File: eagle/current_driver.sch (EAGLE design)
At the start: 46 parts, among them IC4 UA78M05DCY, J1 Hall_Stop, J10 S5, J11 S1, J12 S2, J2 SIG_TEST, J3 S3, J9 S4, K2 4052, Q1 60V/32A/35mΩ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

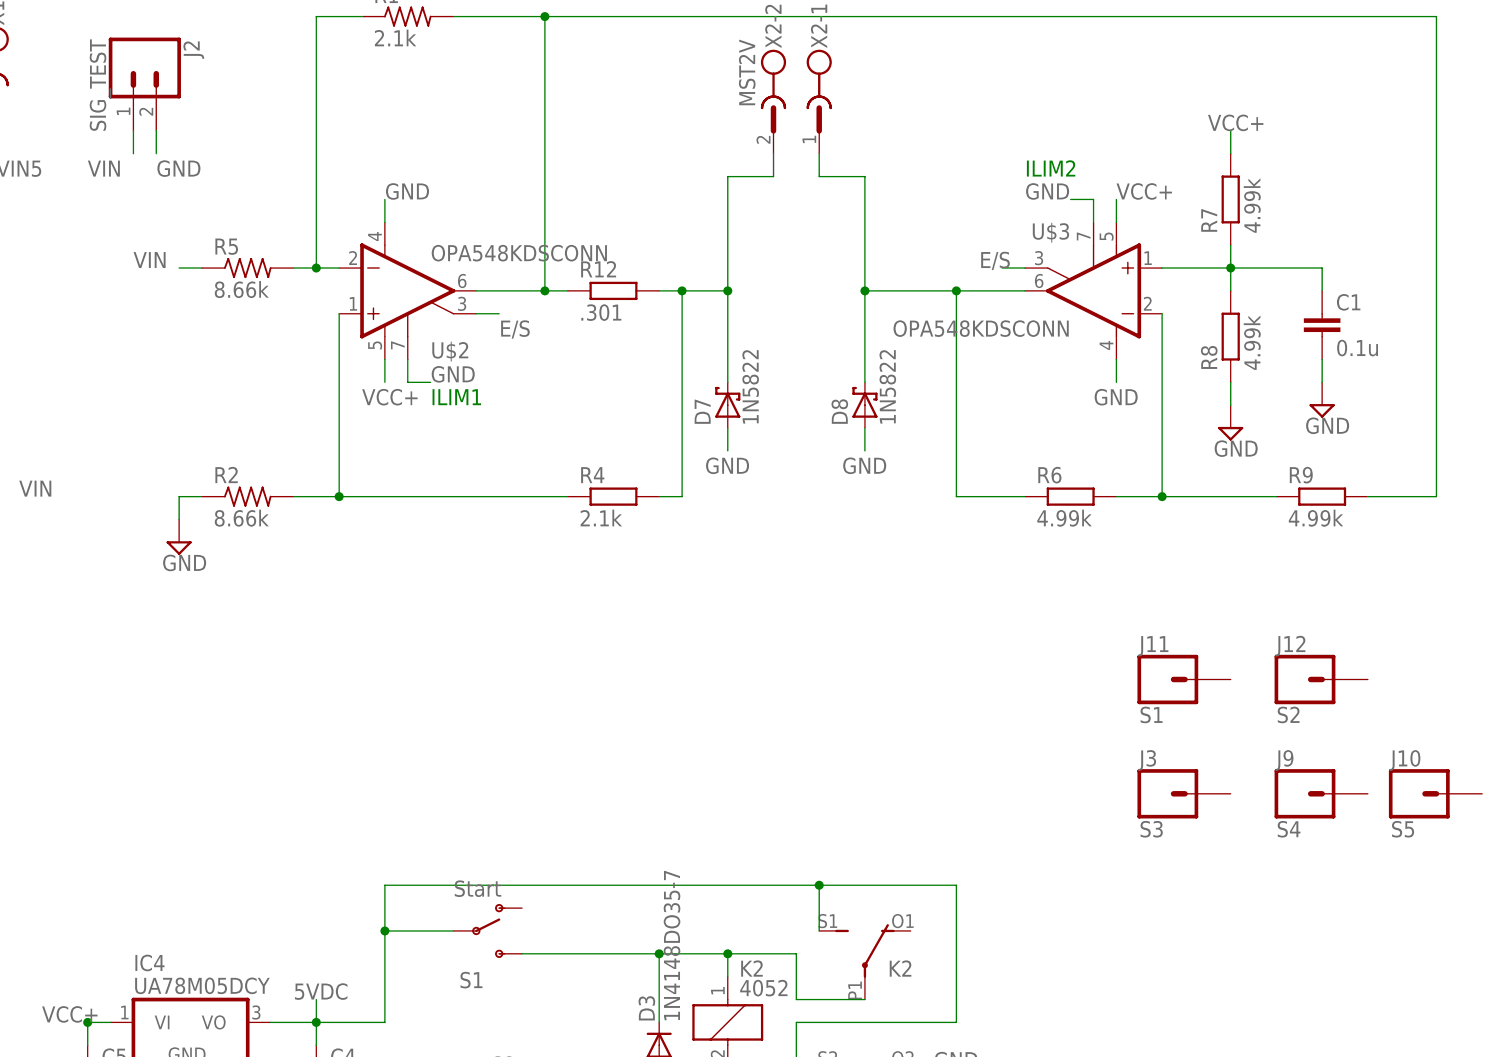
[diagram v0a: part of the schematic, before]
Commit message: modified Rs current sense resistor footprint
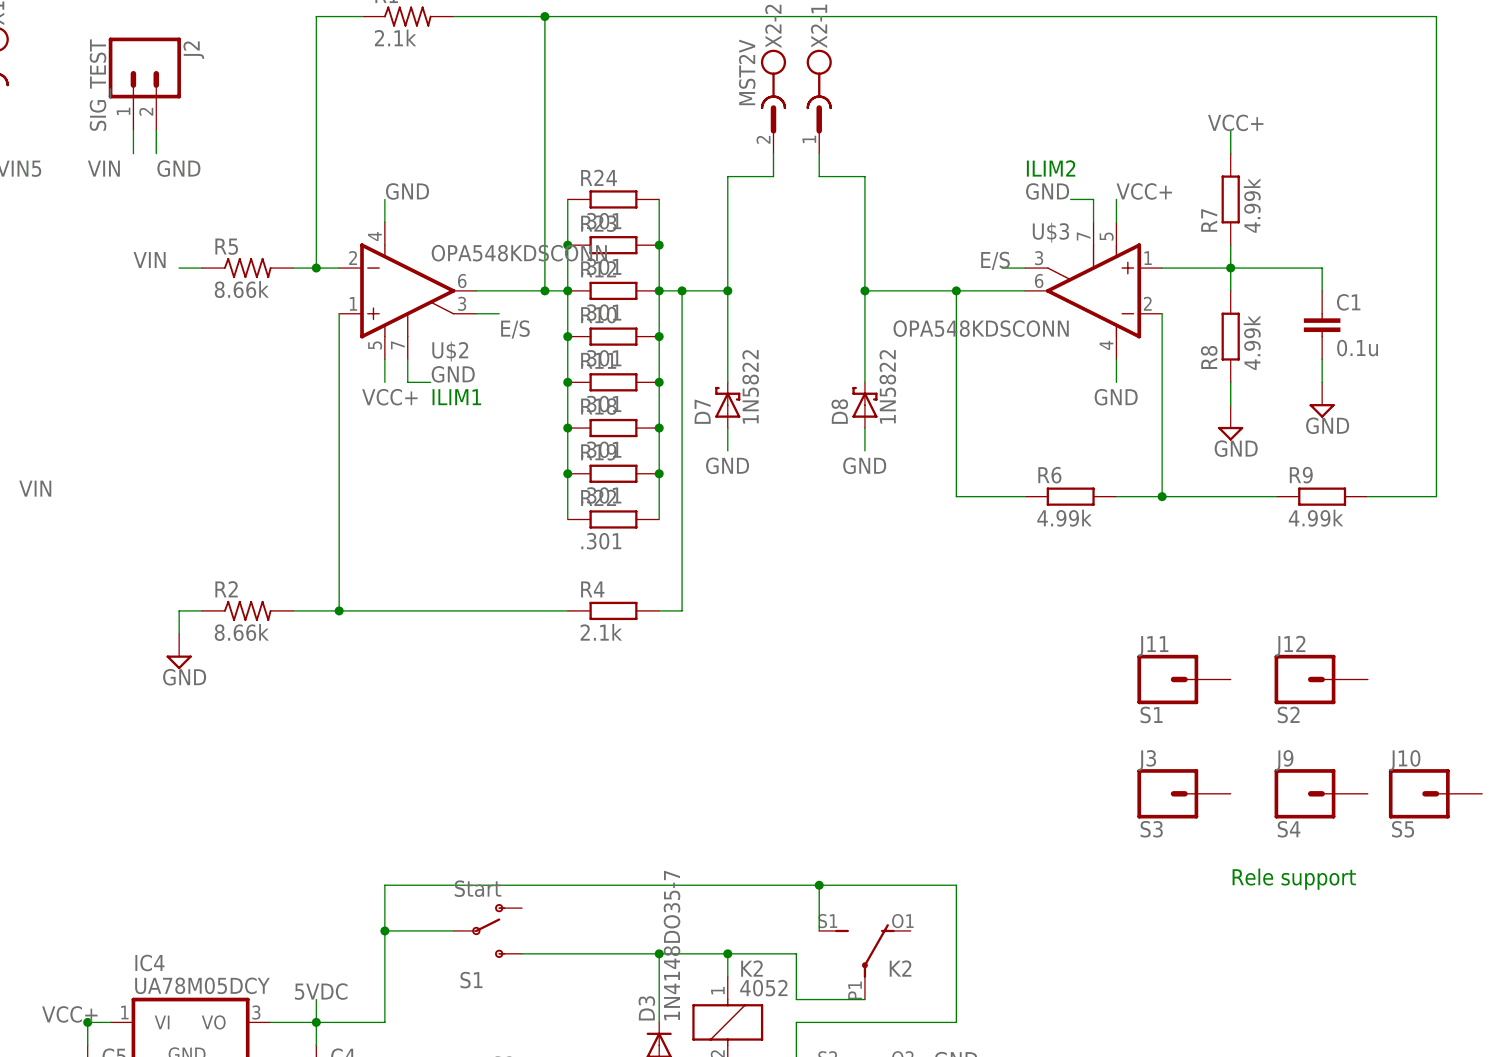
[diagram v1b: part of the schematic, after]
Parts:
- added R10, R11, R18, R19, R22, R23, R24: .301, rcl:R-EU_M1206
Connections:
- removed net N$1: R1.2, R12.1, R9.2, U$2.OUT
- new net N$19: R1.2, R10.1, R11.1, R12.1, R18.1, R19.1, R22.1, R23.1, R24.1, R9.2, U$2.OUT
- net N$3: now also R10.2, R11.2, R18.2, R19.2, R22.2, R23.2, R24.2
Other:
- note added: "Rele support"
- moved on the sheet: R2, R4
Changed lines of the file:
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@@
 <?xml version="1.0" encoding="utf-8"?>
 <!DOCTYPE eagle SYSTEM "eagle.dtd">
-<eagle version="7.2.0">
+<eagle version="8.3.2">
 <drawing>
 <settings>
 <setting alwaysvectorfont="no"/>
+<setting keepoldvectorfont="yes"/>
 <setting verticaltext="up"/>
 </settings>
@@
 <part name="D3" library="diode" deviceset="1N4148" device="DO35-7"/>
 <part name="D4" library="diode" deviceset="1N4148" device="DO35-7"/>
+<part name="R10" library="rcl" deviceset="R-EU_" device="M1206" value=".301"/>
+<part name="R11" library="rcl" deviceset="R-EU_" device="M1206" value=".301"/>
+<part name="R18" library="rcl" deviceset="R-EU_" device="M1206" value=".301"/>
+<part name="R19" library="rcl" deviceset="R-EU_" device="M1206" value=".301"/>
+<part name="R22" library="rcl" deviceset="R-EU_" device="M1206" value=".301"/>
+<part name="R23" library="rcl" deviceset="R-EU_" device="M1206" value=".301"/>
+<part name="R24" library="rcl" deviceset="R-EU_" device="M1206" value=".301"/>
 </parts>
 <sheets>
@@
 <text x="66.04" y="38.1" size="1.778" layer="91">ILIM1</text>
 <text x="132.08" y="63.5" size="1.778" layer="91">ILIM2</text>
+<text x="154.94" y="-15.24" size="1.778" layer="91">Rele support</text>
 </plain>
 <instances>
 <instance part="R1" gate="G$1" x="63.5" y="81.28"/>
-<instance part="R2" gate="G$1" x="45.72" y="27.94"/>
-<instance part="R4" gate="G$1" x="86.36" y="27.94"/>
-<instance part="SUPPLY1" gate="GND" x="38.1" y="22.86"/>
+<instance part="R2" gate="G$1" x="45.72" y="15.24"/>
+<instance part="R4" gate="G$1" x="86.36" y="15.24"/>
+<instance part="SUPPLY1" gate="GND" x="38.1" y="10.16"/>
 <instance part="R5" gate="G$1" x="45.72" y="53.34"/>
 <instance part="R6" gate="G$1" x="137.16" y="27.94"/>
@@
 <instance part="D3" gate="G$1" x="91.44" y="-33.02" rot="R90"/>
 <instance part="D4" gate="G$1" x="86.36" y="-66.04" rot="R180"/>
+<instance part="R10" gate="G$1" x="86.36" y="45.72"/>
+<instance part="R11" gate="G$1" x="86.36" y="40.64"/>
+<instance part="R18" gate="G$1" x="86.36" y="35.56"/>
+<instance part="R19" gate="G$1" x="86.36" y="30.48"/>
+<instance part="R22" gate="G$1" x="86.36" y="25.4"/>
+<instance part="R23" gate="G$1" x="86.36" y="55.88"/>
+<instance part="R24" gate="G$1" x="86.36" y="60.96"/>
 </instances>
 <busses>
 </busses>
 <nets>
-<net name="N$1" class="0">
-<segment>
-<wire x1="71.12" y1="50.8" x2="78.74" y2="50.8" width="0.1524" layer="91"/>
-<wire x1="78.74" y1="50.8" x2="78.74" y2="81.28" width="0.1524" layer="91"/>
-<pinref part="R1" gate="G$1" pin="2"/>
-<wire x1="78.74" y1="81.28" x2="68.58" y2="81.28" width="0.1524" layer="91"/>
-<wire x1="78.74" y1="50.8" x2="81.28" y2="50.8" width="0.1524" layer="91"/>
-<wire x1="177.8" y1="81.28" x2="78.74" y2="81.28" width="0.1524" layer="91"/>
-<wire x1="177.8" y1="81.28" x2="177.8" y2="27.94" width="0.1524" layer="91"/>
-<pinref part="R9" gate="G$1" pin="2"/>
-<wire x1="177.8" y1="27.94" x2="170.18" y2="27.94" width="0.1524" layer="91"/>
-<pinref part="R12" gate="G$1" pin="1"/>
-<junction x="78.74" y="81.28"/>
-<junction x="78.74" y="50.8"/>
-<pinref part="U$2" gate="G$1" pin="OUT"/>
-</segment>
-</net>
 <net name="N$2" class="0">
 <segment>
@@
 <junction x="99.06" y="50.8"/>
 <pinref part="R4" gate="G$1" pin="2"/>
-<wire x1="91.44" y1="27.94" x2="93.98" y2="27.94" width="0.1524" layer="91"/>
-<wire x1="93.98" y1="27.94" x2="93.98" y2="50.8" width="0.1524" layer="91"/>
+<wire x1="91.44" y1="15.24" x2="93.98" y2="15.24" width="0.1524" layer="91"/>
+<wire x1="93.98" y1="15.24" x2="93.98" y2="50.8" width="0.1524" layer="91"/>
 <junction x="93.98" y="50.8"/>
 <wire x1="99.06" y1="63.5" x2="104.14" y2="63.5" width="0.1524" layer="91"/>
@@
 <wire x1="104.14" y1="63.5" x2="104.14" y2="66.04" width="0.1524" layer="91"/>
 <pinref part="D7" gate="G$1" pin="C"/>
+<pinref part="R10" gate="G$1" pin="2"/>
+<wire x1="91.44" y1="45.72" x2="91.44" y2="50.8" width="0.1524" layer="91"/>
+<junction x="91.44" y="50.8"/>
+<pinref part="R11" gate="G$1" pin="2"/>
+<wire x1="91.44" y1="40.64" x2="91.44" y2="45.72" width="0.1524" layer="91"/>
+<junction x="91.44" y="45.72"/>
+<pinref part="R18" gate="G$1" pin="2"/>
+<wire x1="91.44" y1="35.56" x2="91.44" y2="40.64" width="0.1524" layer="91"/>
+<junction x="91.44" y="40.64"/>
+<pinref part="R19" gate="G$1" pin="2"/>
+<wire x1="91.44" y1="30.48" x2="91.44" y2="35.56" width="0.1524" layer="91"/>
+<junction x="91.44" y="35.56"/>
+<pinref part="R22" gate="G$1" pin="2"/>
+<wire x1="91.44" y1="25.4" x2="91.44" y2="30.48" width="0.1524" layer="91"/>
+<junction x="91.44" y="30.48"/>
+<pinref part="R23" gate="G$1" pin="2"/>
+<wire x1="91.44" y1="55.88" x2="91.44" y2="50.8" width="0.1524" layer="91"/>
+<pinref part="R24" gate="G$1" pin="2"/>
+<wire x1="91.44" y1="60.96" x2="91.44" y2="55.88" width="0.1524" layer="91"/>
+<junction x="91.44" y="55.88"/>
 </segment>
 </net>
@@
 <segment>
 <pinref part="R4" gate="G$1" pin="1"/>
-<wire x1="81.28" y1="27.94" x2="55.88" y2="27.94" width="0.1524" layer="91"/>
-<wire x1="55.88" y1="27.94" x2="55.88" y2="48.26" width="0.1524" layer="91"/>
+<wire x1="81.28" y1="15.24" x2="55.88" y2="15.24" width="0.1524" layer="91"/>
+<wire x1="55.88" y1="15.24" x2="55.88" y2="48.26" width="0.1524" layer="91"/>
 <pinref part="R2" gate="G$1" pin="2"/>
-<wire x1="50.8" y1="27.94" x2="55.88" y2="27.94" width="0.1524" layer="91"/>
-<junction x="55.88" y="27.94"/>
+<wire x1="50.8" y1="15.24" x2="55.88" y2="15.24" width="0.1524" layer="91"/>
+<junction x="55.88" y="15.24"/>
 <pinref part="U$2" gate="G$1" pin="+IN"/>
 </segment>
@@
 <segment>
 <pinref part="R2" gate="G$1" pin="1"/>
-<wire x1="40.64" y1="27.94" x2="38.1" y2="27.94" width="0.1524" layer="91"/>
-<wire x1="38.1" y1="27.94" x2="38.1" y2="25.4" width="0.1524" layer="91"/>
+<wire x1="40.64" y1="15.24" x2="38.1" y2="15.24" width="0.1524" layer="91"/>
+<wire x1="38.1" y1="15.24" x2="38.1" y2="12.7" width="0.1524" layer="91"/>
 <pinref part="SUPPLY1" gate="GND" pin="GND"/>
 </segment>
@@
 </segment>
 </net>
+<net name="N$19" class="0">
+<segment>
+<pinref part="R24" gate="G$1" pin="1"/>
+<pinref part="R23" gate="G$1" pin="1"/>
+<wire x1="81.28" y1="60.96" x2="81.28" y2="55.88" width="0.1524" layer="91"/>
+<pinref part="R22" gate="G$1" pin="1"/>
+<pinref part="R19" gate="G$1" pin="1"/>
+<wire x1="81.28" y1="25.4" x2="81.28" y2="30.48" width="0.1524" layer="91"/>
+<pinref part="R18" gate="G$1" pin="1"/>
+<wire x1="81.28" y1="35.56" x2="81.28" y2="30.48" width="0.1524" layer="91"/>
+<junction x="81.28" y="30.48"/>
+<pinref part="R11" gate="G$1" pin="1"/>
+<wire x1="81.28" y1="35.56" x2="81.28" y2="40.64" width="0.1524" layer="91"/>
+<junction x="81.28" y="35.56"/>
+<pinref part="R10" gate="G$1" pin="1"/>
+<wire x1="81.28" y1="45.72" x2="81.28" y2="40.64" width="0.1524" layer="91"/>
+<junction x="81.28" y="40.64"/>
+<wire x1="71.12" y1="50.8" x2="78.74" y2="50.8" width="0.1524" layer="91"/>
+<wire x1="78.74" y1="50.8" x2="78.74" y2="81.28" width="0.1524" layer="91"/>
+<pinref part="R1" gate="G$1" pin="2"/>
+<wire x1="78.74" y1="81.28" x2="68.58" y2="81.28" width="0.1524" layer="91"/>
+<wire x1="78.74" y1="50.8" x2="81.28" y2="50.8" width="0.1524" layer="91"/>
+<wire x1="177.8" y1="81.28" x2="78.74" y2="81.28" width="0.1524" layer="91"/>
+<wire x1="177.8" y1="81.28" x2="177.8" y2="27.94" width="0.1524" layer="91"/>
+<pinref part="R9" gate="G$1" pin="2"/>
+<wire x1="177.8" y1="27.94" x2="170.18" y2="27.94" width="0.1524" layer="91"/>
+<pinref part="R12" gate="G$1" pin="1"/>
+<junction x="78.74" y="81.28"/>
+<junction x="78.74" y="50.8"/>
+<pinref part="U$2" gate="G$1" pin="OUT"/>
+<wire x1="81.28" y1="45.72" x2="81.28" y2="50.8" width="0.1524" layer="91"/>
+<junction x="81.28" y="45.72"/>
+<junction x="81.28" y="50.8"/>
+<wire x1="81.28" y1="55.88" x2="81.28" y2="50.8" width="0.1524" layer="91"/>
+<junction x="81.28" y="55.88"/>
+</segment>
+</net>
 </nets>
 </sheet>
 </sheets>
+<errors>
+</errors>
 </schematic>
 </drawing>
